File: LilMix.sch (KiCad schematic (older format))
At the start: 58 parts, among them J1_L1 MONO, J1_R1 MONO, J2_L1 MONO, J2_R1 MONO, J3 STEREO, J4 MONO, J5 MONO, J6 STEREO, J7 MONO, U1 TL074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

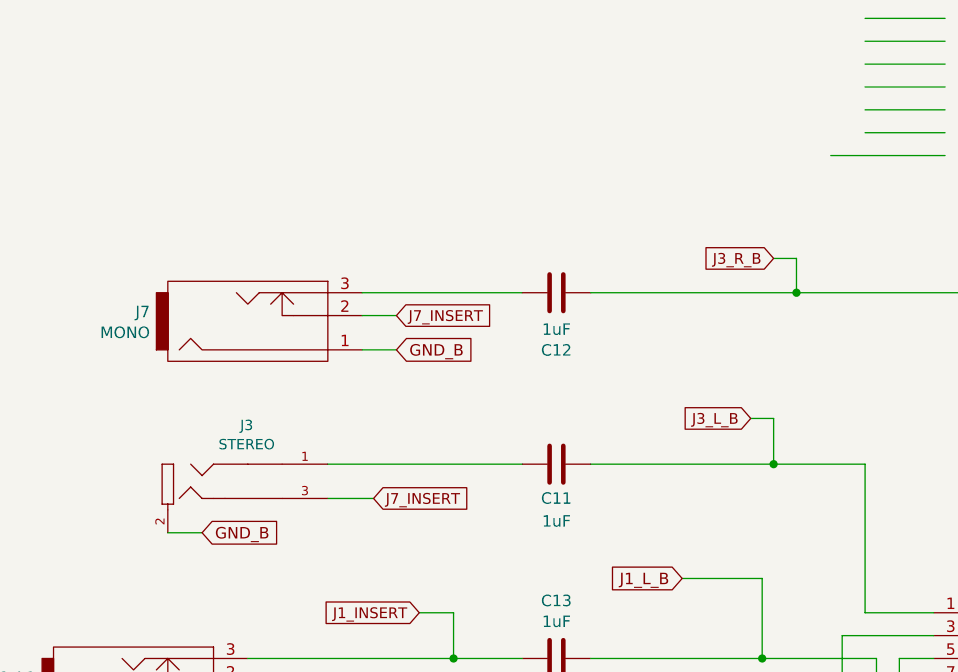
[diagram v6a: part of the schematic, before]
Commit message: Add header pins to chose normal options on channel 3
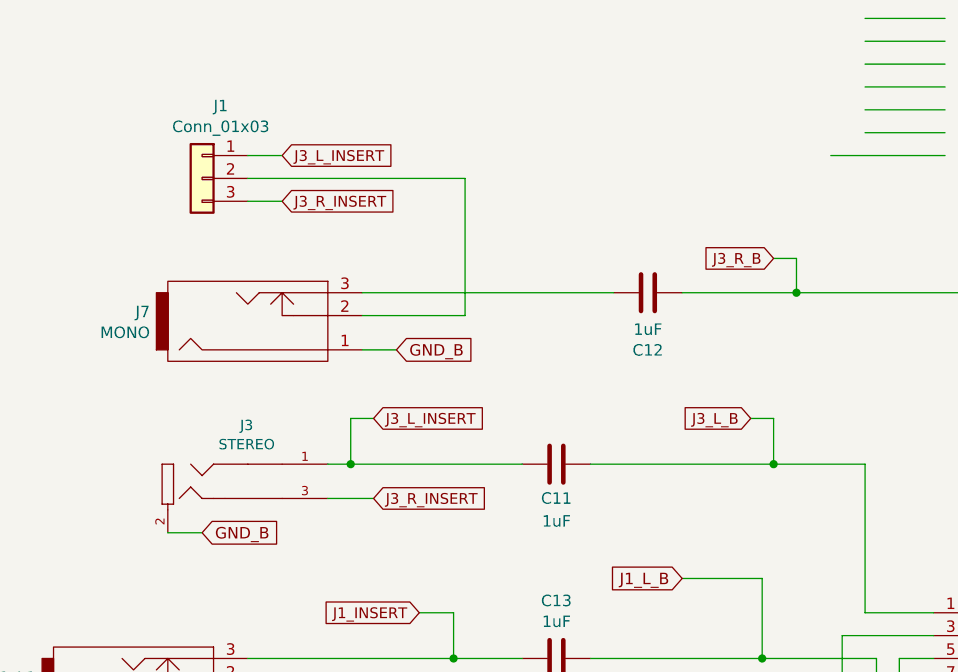
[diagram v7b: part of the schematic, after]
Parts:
- added J1: Conn_01x03, Connector_PinHeader_2.54mm:PinHeader_1x03_P2.54mm_Vertical, symbol Connector_Generic:Conn_01x03
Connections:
- net labels added: J3_L_INSERT, J3_R_INSERT
- net labels removed: J7_INSERT
- wire segments 327 -> 334
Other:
- moved on the sheet: C12
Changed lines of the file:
@@
 EESchema Schematic File Version 4
+LIBS:LilMix-cache
 EELAYER 30 0
 EELAYER END
@@
 L 4ms-passives:C C12
 U 1 1 5E77E136
-P -5700 1750
-F 0 "C12" V -5952 1750 50  0000 C CNN
-F 1 "1uF" V -5861 1750 50  0000 C CNN
-F 2 "Capacitor_THT:C_Rect_L7.0mm_W4.5mm_P5.00mm" H -5662 1600 50  0001 C CNN
-F 3 "" H -5700 1750 50  0001 C CNN
-	1    -5700 1750
+P -5300 1750
+F 0 "C12" V -5552 1750 50  0000 C CNN
+F 1 "1uF" V -5461 1750 50  0000 C CNN
+F 2 "Capacitor_THT:C_Rect_L7.0mm_W4.5mm_P5.00mm" H -5262 1600 50  0001 C CNN
+F 3 "" H -5300 1750 50  0001 C CNN
+	1    -5300 1750
 	0    -1   -1   0
 $EndComp
@@
 	-1400 4000 -1400 4850
 Wire Wire Line
-	-5550 1750 -4650 1750
+	-5150 1750 -4650 1750
 Wire Wire Line
 	-1600 4300 -1600 4950
@@
 	-1450 4700 -1450 4750
 Wire Wire Line
-	-6700 2500 -5850 2500
+	-6700 2500 -6600 2500
 Connection ~ -1800 4750
 Wire Wire Line
@@
 	-6700 2650 -6500 2650
 Text GLabel -6500 2650 2    47   Input ~ 0
-J7_INSERT
+J3_R_INSERT
 Wire Wire Line
 	-6550 2000 -6400 2000
@@
 GND_B
 Wire Wire Line
-	-6550 1750 -5850 1750
-Wire Wire Line
-	-6550 1850 -6400 1850
-Text GLabel -6400 1850 2    47   Input ~ 0
-J7_INSERT
+	-7050 1350 -6900 1350
+Text GLabel -6900 1350 2    47   Input ~ 0
+J3_R_INSERT
 $Comp
 L eurocad:PJ301M-12 J7
@@
 Wire Wire Line
 	-6150 3350 -5850 3350
+Wire Wire Line
+	-6550 1750 -5450 1750
+Wire Wire Line
+	-7050 1250 -6100 1250
+Wire Wire Line
+	-6100 1250 -6100 1850
+Wire Wire Line
+	-6550 1850 -6100 1850
+$Comp
+L Connector_Generic:Conn_01x03 J1
+U 1 1 5E85B730
+P -7250 1250
+F 0 "J1" H -7332 1567 50  0000 C CNN
+F 1 "Conn_01x03" H -7332 1476 50  0000 C CNN
+F 2 "Connector_PinHeader_2.54mm:PinHeader_1x03_P2.54mm_Vertical" H -7250 1250 50  0001 C CNN
+F 3 "~" H -7250 1250 50  0001 C CNN
+	1    -7250 1250
+	-1   0    0    -1
+$EndComp
+Text GLabel -6500 2300 2    47   Input ~ 0
+J3_L_INSERT
+Wire Wire Line
+	-6600 2300 -6600 2500
+Wire Wire Line
+	-6600 2300 -6500 2300
+Connection ~ -6600 2500
+Wire Wire Line
+	-6600 2500 -5850 2500
+Text GLabel -6900 1150 2    47   Input ~ 0
+J3_L_INSERT
+Wire Wire Line
+	-7050 1150 -6900 1150
 $EndSCHEMATC

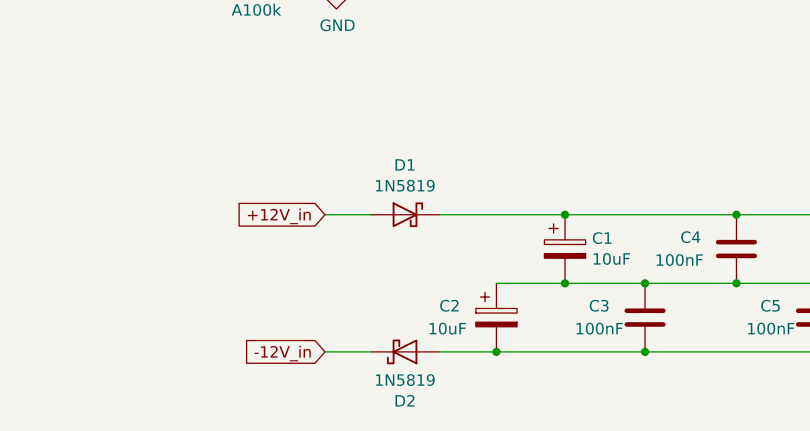
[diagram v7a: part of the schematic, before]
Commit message: Change diode values
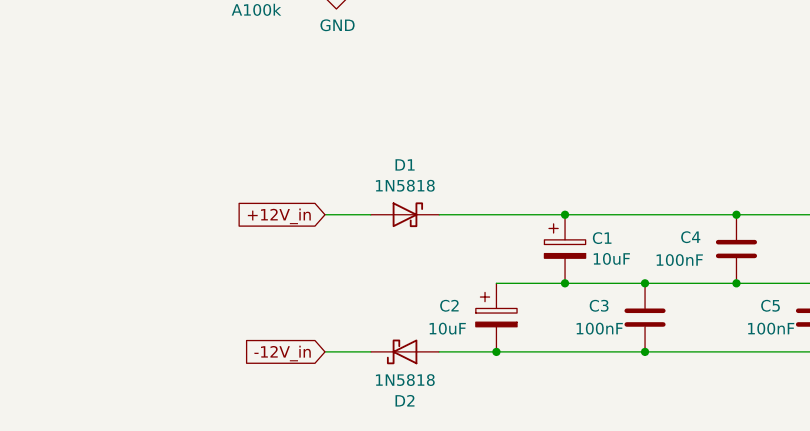
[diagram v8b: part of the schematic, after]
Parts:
- D1, D2: value 1N5819 -> 1N5818
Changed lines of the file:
@@
 P 2250 7700
 F 0 "D2" H 2250 7916 50  0000 C CNN
-F 1 "1N5819" H 2250 7825 50  0000 C CNN
+F 1 "1N5818" H 2250 7825 50  0000 C CNN
 F 2 "Diode_SMD:D_SOD-123" H 2250 7700 50  0001 C CNN
 F 3 "" H 2250 7700 50  0001 C CNN
@@
 P 2250 7100
 F 0 "D1" H 2250 7316 50  0000 C CNN
-F 1 "1N5819" H 2250 7225 50  0000 C CNN
+F 1 "1N5818" H 2250 7225 50  0000 C CNN
 F 2 "Diode_SMD:D_SOD-123" H 2250 7100 50  0001 C CNN
 F 3 "" H 2250 7100 50  0001 C CNN
